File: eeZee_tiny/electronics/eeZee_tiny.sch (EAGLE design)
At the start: 8 parts, among them IC1 attiny, J2 avrisp

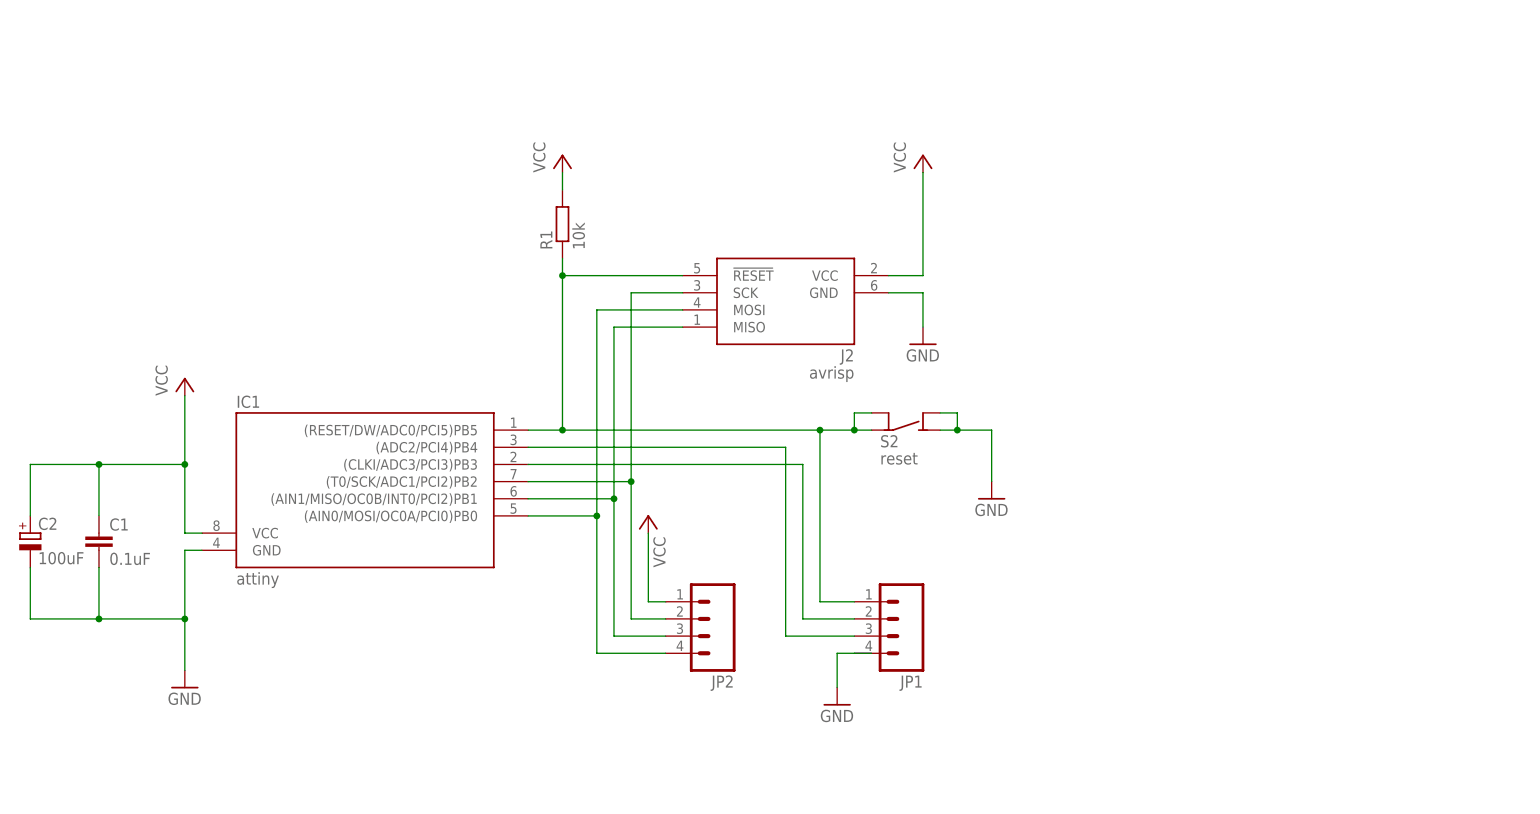
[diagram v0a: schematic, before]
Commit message: Moved caps, mods to routing, added logos, added SCK indicator mark
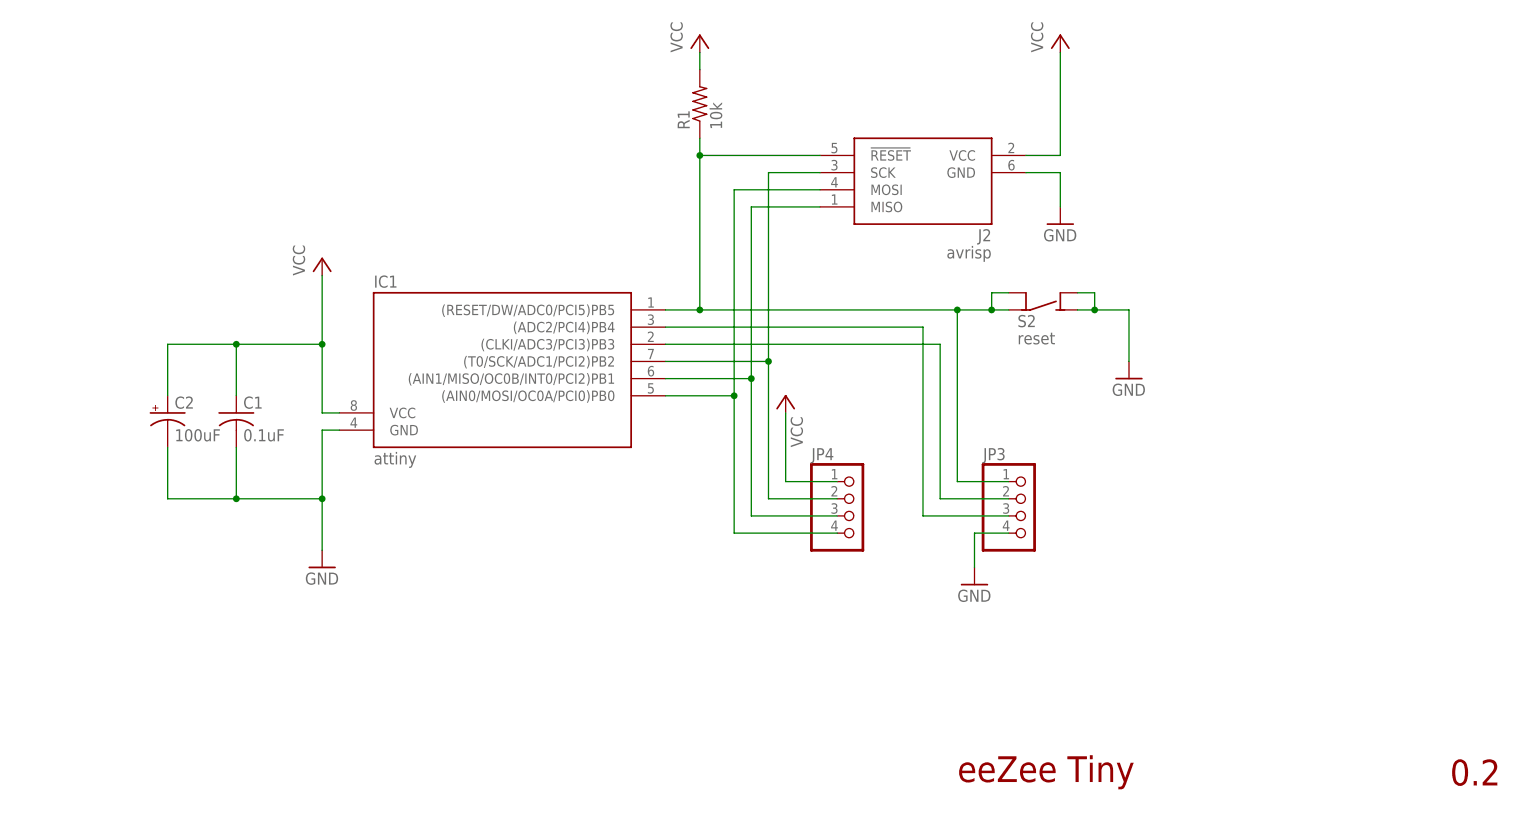
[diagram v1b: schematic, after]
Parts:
- removed JP1, JP2: (no value), SparkFun:M04PTH
- added JP3, JP4: (no value), pinhead-2:PINHD-1X04_2.54-S
- C1: device rcl:C-EUC0603 -> rcl:C-USC0603
- C2: device rcl:CPOL-EUSMCB -> rcl:CPOL-USSMCB
- R1: device rcl:R-EU_R0603 -> rcl:R-US_R0603
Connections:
- net !RESET: now also JP3.1; no longer JP1.1
- net GND: now also JP3.4; no longer JP1.4
- net MISO: now also JP4.3; no longer JP2.3
- net MOSI: now also JP4.4; no longer JP2.4
- net N$2: now also JP3.2; no longer JP1.2
- net N$8: now also JP3.3; no longer JP1.3
- net SCK: now also JP4.2; no longer JP2.2
- net VCC: now also JP4.1; no longer JP2.1
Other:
- note added: "0.2"
- note added: "eeZee Tiny"
- moved on the sheet: C1, C2, IC1, J2, S2

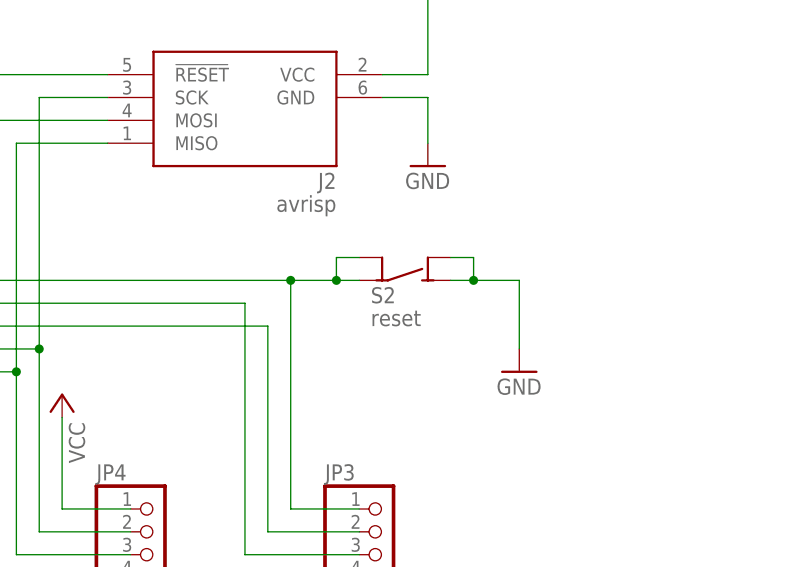
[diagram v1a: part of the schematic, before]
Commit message: Revised layout to reduce leading edge and side edge clearances for better breadboarding.
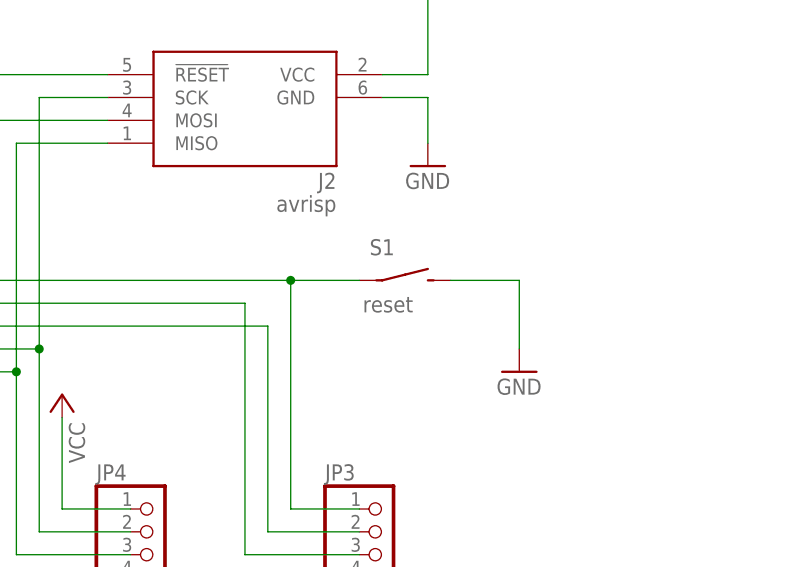
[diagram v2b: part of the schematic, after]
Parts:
- removed S2: reset, mes_electromech:SPST4
- added S1: reset, mes_electromech:SPST_TAC_RECT1
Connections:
- net !RESET: now also S1.P; no longer S2.COM@1, S2.COM@2
- net GND: now also S1.S; no longer S2.NO@1, S2.NO@2
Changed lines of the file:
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@@
 </part>
 <part name="J2" library="ads4" deviceset="AVRISP6" device="" value="avrisp"/>
-<part name="S2" library="mes_electromech" deviceset="SPST4" device="" value="reset"/>
 <part name="JP3" library="pinhead-2" deviceset="PINHD-1X04" device="_2.54-S"/>
 <part name="JP4" library="pinhead-2" deviceset="PINHD-1X04" device="_2.54-S"/>
 <part name="FRAME1" library="mes" deviceset="LETTER_L" device=""/>
+<part name="S1" library="mes_electromech" deviceset="SPST" device="_TAC_RECT1" value="reset"/>
 </parts>
 <sheets>
@@
 </instance>
 <instance part="J2" gate="A" x="154.94" y="109.22" rot="MR0"/>
-<instance part="S2" gate="G$1" x="172.72" y="93.98"/>
 <instance part="JP3" gate="A" x="170.18" y="63.5"/>
 <instance part="JP4" gate="A" x="144.78" y="63.5"/>
 <instance part="FRAME1" gate="G$1" x="0" y="0"/>
 <instance part="FRAME1" gate="G$2" x="147.32" y="2.54"/>
+<instance part="S1" gate="G$1" x="172.72" y="93.98"/>
 </instances>
 <busses>
@@
 <segment>
 <wire x1="185.42" y1="86.36" x2="185.42" y2="93.98" width="0.1524" layer="91"/>
-<wire x1="185.42" y1="93.98" x2="180.34" y2="93.98" width="0.1524" layer="91"/>
+<wire x1="185.42" y1="93.98" x2="177.8" y2="93.98" width="0.1524" layer="91"/>
 <pinref part="GND3" gate="1" pin="GND"/>
-<pinref part="S2" gate="G$1" pin="NO@1"/>
-<pinref part="S2" gate="G$1" pin="NO@2"/>
-<wire x1="180.34" y1="93.98" x2="177.8" y2="93.98" width="0.1524" layer="91"/>
-<wire x1="177.8" y1="96.52" x2="180.34" y2="96.52" width="0.1524" layer="91"/>
-<wire x1="180.34" y1="96.52" x2="180.34" y2="93.98" width="0.1524" layer="91"/>
-<junction x="180.34" y="93.98"/>
+<pinref part="S1" gate="G$1" pin="S"/>
 </segment>
 <segment>
@@
 <pinref part="IC1" gate="G$1" pin="(RESET/DW/ADC0/PCI5)PB5"/>
 <pinref part="R1" gate="G$1" pin="1"/>
-<wire x1="167.64" y1="93.98" x2="165.1" y2="93.98" width="0.1524" layer="91"/>
 <junction x="160.02" y="93.98"/>
 <pinref part="J2" gate="A" pin="!RESET"/>
-<pinref part="S2" gate="G$1" pin="COM@1"/>
-<pinref part="S2" gate="G$1" pin="COM@2"/>
-<wire x1="165.1" y1="93.98" x2="160.02" y2="93.98" width="0.1524" layer="91"/>
-<wire x1="167.64" y1="96.52" x2="165.1" y2="96.52" width="0.1524" layer="91"/>
-<wire x1="165.1" y1="96.52" x2="165.1" y2="93.98" width="0.1524" layer="91"/>
-<junction x="165.1" y="93.98"/>
+<wire x1="167.64" y1="93.98" x2="160.02" y2="93.98" width="0.1524" layer="91"/>
 <pinref part="JP3" gate="A" pin="1"/>
+<pinref part="S1" gate="G$1" pin="P"/>
 </segment>
 </net>

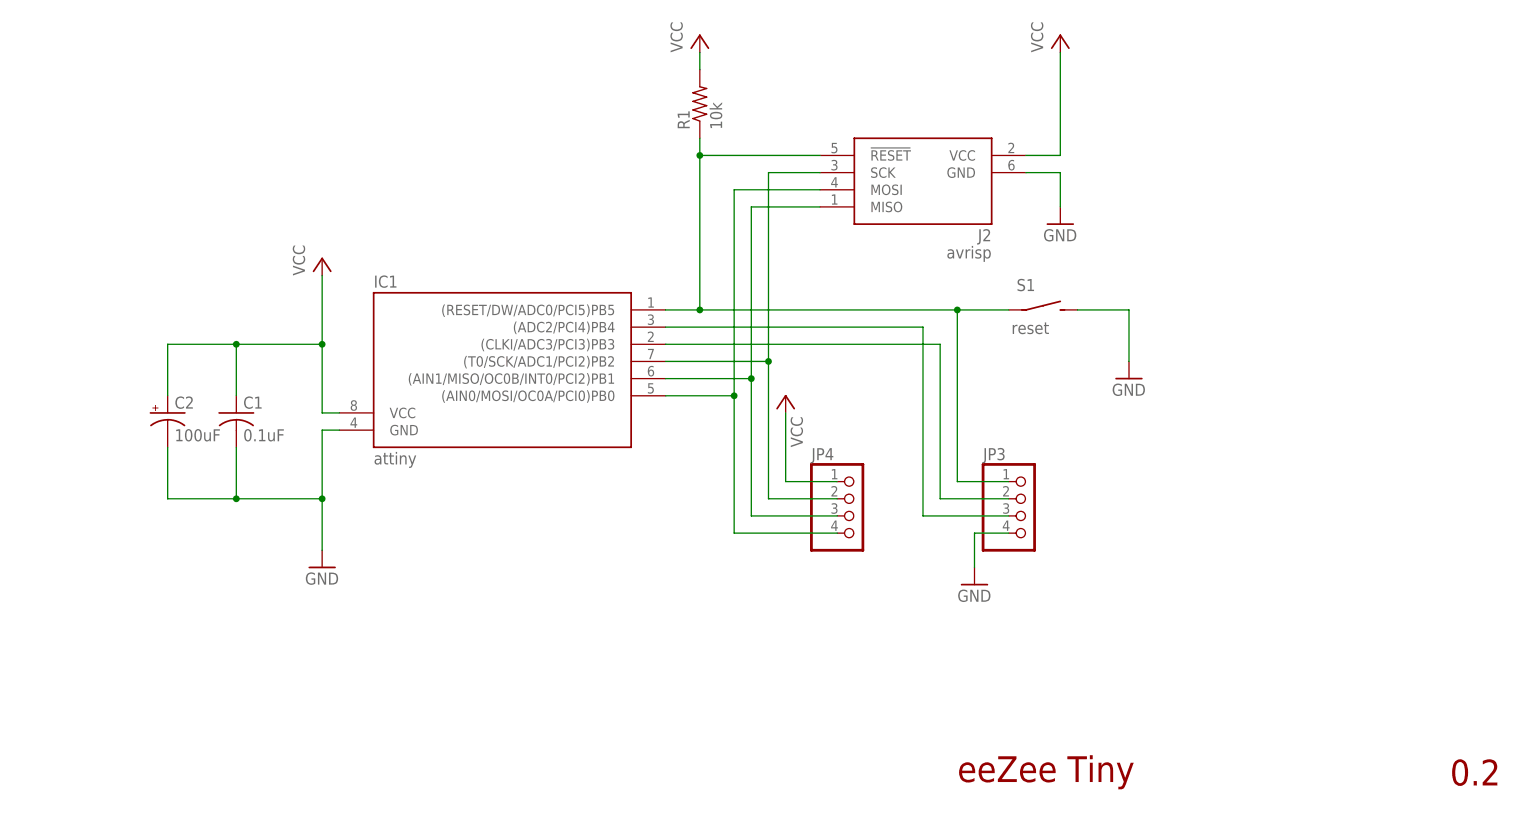
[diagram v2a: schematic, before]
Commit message: Rev 0.2, shrunk board, mitered corners, added polarity silk to tantalum.
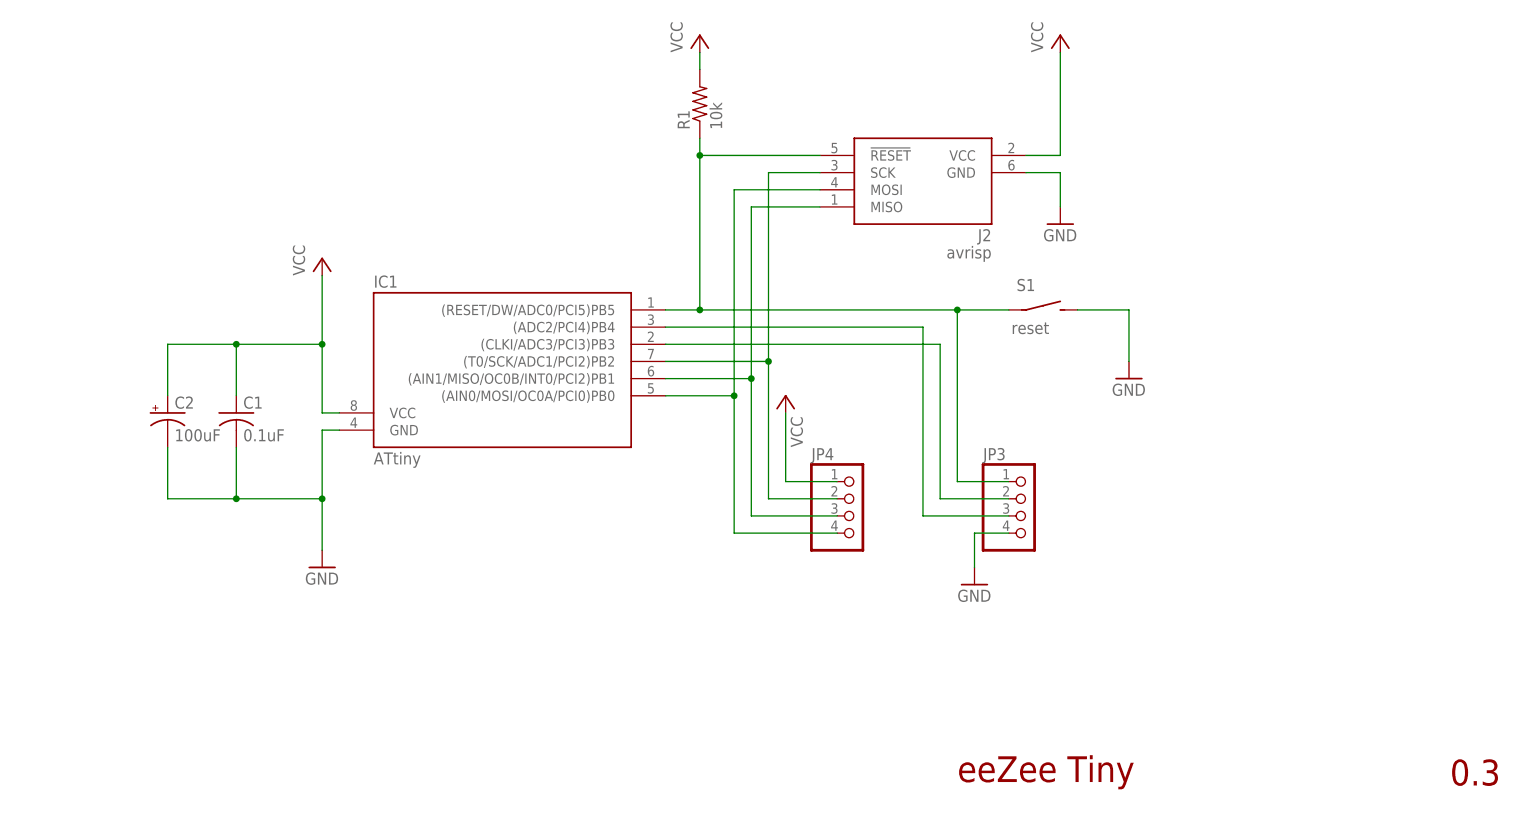
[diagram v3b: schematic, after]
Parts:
- C2: device rcl:CPOL-USSMCB -> mes_rcl:CAP_POL_SMC_B
- IC1: value attiny -> ATtiny
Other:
- note added: "0.3"
- note removed: "0.2"
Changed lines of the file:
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@@
 <?xml version="1.0" encoding="utf-8"?>
 <!DOCTYPE eagle SYSTEM "eagle.dtd">
-<eagle version="6.3">
+<eagle version="6.4">
 <drawing>
 <settings>
@@
 <grid distance="0.1" unitdist="inch" unit="inch" style="lines" multiple="1" display="no" altdistance="0.01" altunitdist="inch" altunit="inch"/>
 <layers>
-<layer number="1" name="Top" color="4" fill="1" visible="no" active="no"/>
-<layer number="16" name="Bottom" color="1" fill="1" visible="no" active="no"/>
-<layer number="17" name="Pads" color="2" fill="1" visible="no" active="no"/>
-<layer number="18" name="Vias" color="2" fill="1" visible="no" active="no"/>
-<layer number="19" name="Unrouted" color="6" fill="1" visible="no" active="no"/>
-<layer number="20" name="Dimension" color="15" fill="1" visible="no" active="no"/>
-<layer number="21" name="tPlace" color="7" fill="1" visible="no" active="no"/>
-<layer number="22" name="bPlace" color="7" fill="1" visible="no" active="no"/>
-<layer number="23" name="tOrigins" color="15" fill="1" visible="no" active="no"/>
-<layer number="24" name="bOrigins" color="15" fill="1" visible="no" active="no"/>
-<layer number="25" name="tNames" color="7" fill="1" visible="no" active="no"/>
-<layer number="26" name="bNames" color="7" fill="1" visible="no" active="no"/>
-<layer number="27" name="tValues" color="7" fill="1" visible="no" active="no"/>
-<layer number="28" name="bValues" color="7" fill="1" visible="no" active="no"/>
+<layer number="1" name="Top" color="4" fill="1" visible="yes" active="no"/>
+<layer number="16" name="Bottom" color="1" fill="1" visible="yes" active="no"/>
+<layer number="17" name="Pads" color="2" fill="1" visible="yes" active="no"/>
+<layer number="18" name="Vias" color="2" fill="1" visible="yes" active="no"/>
+<layer number="19" name="Unrouted" color="6" fill="1" visible="yes" active="no"/>
+<layer number="20" name="Dimension" color="15" fill="1" visible="yes" active="no"/>
+<layer number="21" name="tPlace" color="7" fill="1" visible="yes" active="no"/>
+<layer number="22" name="bPlace" color="7" fill="1" visible="yes" active="no"/>
+<layer number="23" name="tOrigins" color="15" fill="1" visible="yes" active="no"/>
+<layer number="24" name="bOrigins" color="15" fill="1" visible="yes" active="no"/>
+<layer number="25" name="tNames" color="7" fill="1" visible="yes" active="no"/>
+<layer number="26" name="bNames" color="7" fill="1" visible="yes" active="no"/>
+<layer number="27" name="tValues" color="7" fill="1" visible="yes" active="no"/>
+<layer number="28" name="bValues" color="7" fill="1" visible="yes" active="no"/>
 <layer number="29" name="tStop" color="7" fill="3" visible="no" active="no"/>
 <layer number="30" name="bStop" color="7" fill="6" visible="no" active="no"/>
@@
 <layer number="35" name="tGlue" color="7" fill="4" visible="no" active="no"/>
 <layer number="36" name="bGlue" color="7" fill="5" visible="no" active="no"/>
-<layer number="37" name="tTest" color="7" fill="1" visible="no" active="no"/>
-<layer number="38" name="bTest" color="7" fill="1" visible="no" active="no"/>
+<layer number="37" name="tTest" color="7" fill="1" visible="yes" active="no"/>
+<layer number="38" name="bTest" color="7" fill="1" visible="yes" active="no"/>
 <layer number="39" name="tKeepout" color="4" fill="11" visible="no" active="no"/>
 <layer number="40" name="bKeepout" color="1" fill="11" visible="no" active="no"/>
@@
 <layer number="44" name="Drills" color="7" fill="1" visible="no" active="no"/>
 <layer number="45" name="Holes" color="7" fill="1" visible="no" active="no"/>
-<layer number="46" name="Milling" color="3" fill="1" visible="no" active="no"/>
-<layer number="47" name="Measures" color="7" fill="1" visible="no" active="no"/>
-<layer number="48" name="Document" color="7" fill="1" visible="no" active="no"/>
-<layer number="49" name="Reference" color="7" fill="1" visible="no" active="no"/>
-<layer number="50" name="dxf" color="7" fill="1" visible="no" active="no"/>
-<layer number="51" name="tDocu" color="7" fill="1" visible="no" active="no"/>
-<layer number="52" name="bDocu" color="7" fill="1" visible="no" active="no"/>
-<layer number="53" name="tGND_GNDA" color="7" fill="9" visible="no" active="no"/>
-<layer number="54" name="bGND_GNDA" color="1" fill="9" visible="no" active="no"/>
-<layer number="56" name="wert" color="7" fill="1" visible="no" active="no"/>
+<layer number="46" name="Milling" color="3" fill="1" visible="yes" active="no"/>
+<layer number="47" name="Measures" color="7" fill="1" visible="yes" active="no"/>
+<layer number="48" name="Document" color="7" fill="1" visible="yes" active="no"/>
+<layer number="49" name="Reference" color="7" fill="1" visible="yes" active="no"/>
+<layer number="50" name="dxf" color="7" fill="1" visible="yes" active="no"/>
+<layer number="51" name="tDocu" color="7" fill="1" visible="yes" active="no"/>
+<layer number="52" name="bDocu" color="7" fill="1" visible="yes" active="no"/>
+<layer number="53" name="tGND_GNDA" color="7" fill="9" visible="yes" active="no"/>
+<layer number="54" name="bGND_GNDA" color="1" fill="9" visible="yes" active="no"/>
+<layer number="56" name="wert" color="7" fill="1" visible="yes" active="no"/>
 <layer number="91" name="Nets" color="2" fill="1" visible="yes" active="yes"/>
 <layer number="92" name="Busses" color="1" fill="1" visible="yes" active="yes"/>
@@
 <attribute name="PARTNO" value="0603YC104KAT2A"/>
 </part>
-<part name="IC1" library="avr" deviceset="ATTINY13" device="P" technology="-20" value="attiny">
+<part name="IC1" library="avr" deviceset="ATTINY13" device="P" technology="-20" value="ATtiny">
 <attribute name="PARTNO" value="A08-LC-TT-R"/>
 </part>
@@
 <part name="GND6" library="supply1" deviceset="GND" device=""/>
 <part name="P+4" library="supply1" deviceset="VCC" device=""/>
-<part name="C2" library="rcl" deviceset="CPOL-US" device="SMCB" value="100uF">
+<part name="C2" library="mes_rcl" deviceset="CAP_POL" device="_SMC_B" value="100uF">
 <attribute name="BOM" value="INCLUDE"/>
 <attribute name="PARTNO" value="F930J107MBA"/>
@@
 <plain>
 <text x="160.02" y="24.13" size="3.81" layer="94">eeZee Tiny</text>
-<text x="232.918" y="23.622" size="3.81" layer="94">0.2</text>
+<text x="232.918" y="23.622" size="3.81" layer="94">0.3</text>
 </plain>
 <instances>
